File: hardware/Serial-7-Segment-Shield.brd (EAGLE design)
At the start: 59.7 x 53.3 mm, 32 parts, among them J1 AVR_SPI_PRG_6PTH, U1 ARDUINO_SHIELDLABEL

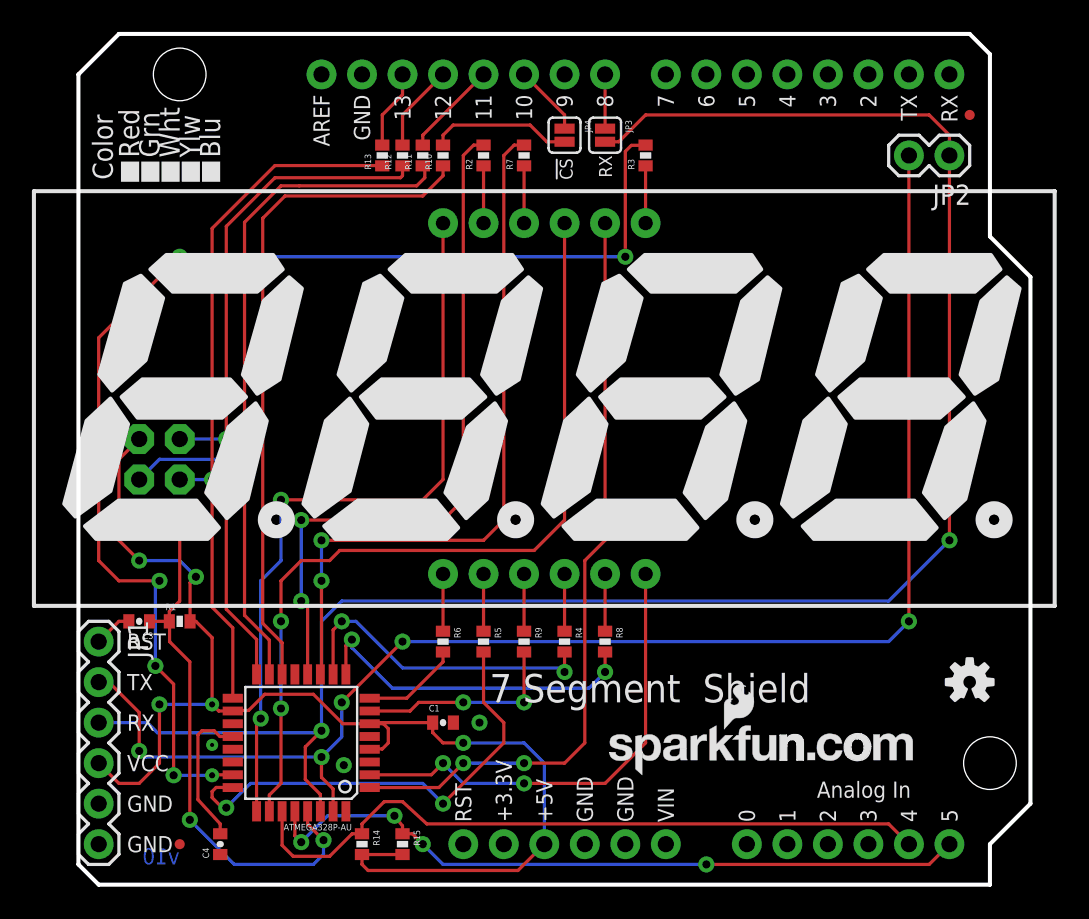
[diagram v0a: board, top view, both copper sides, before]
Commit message: 0603 Cap/Res Change
Changed all caps and res to 0603, minor trace re-routing
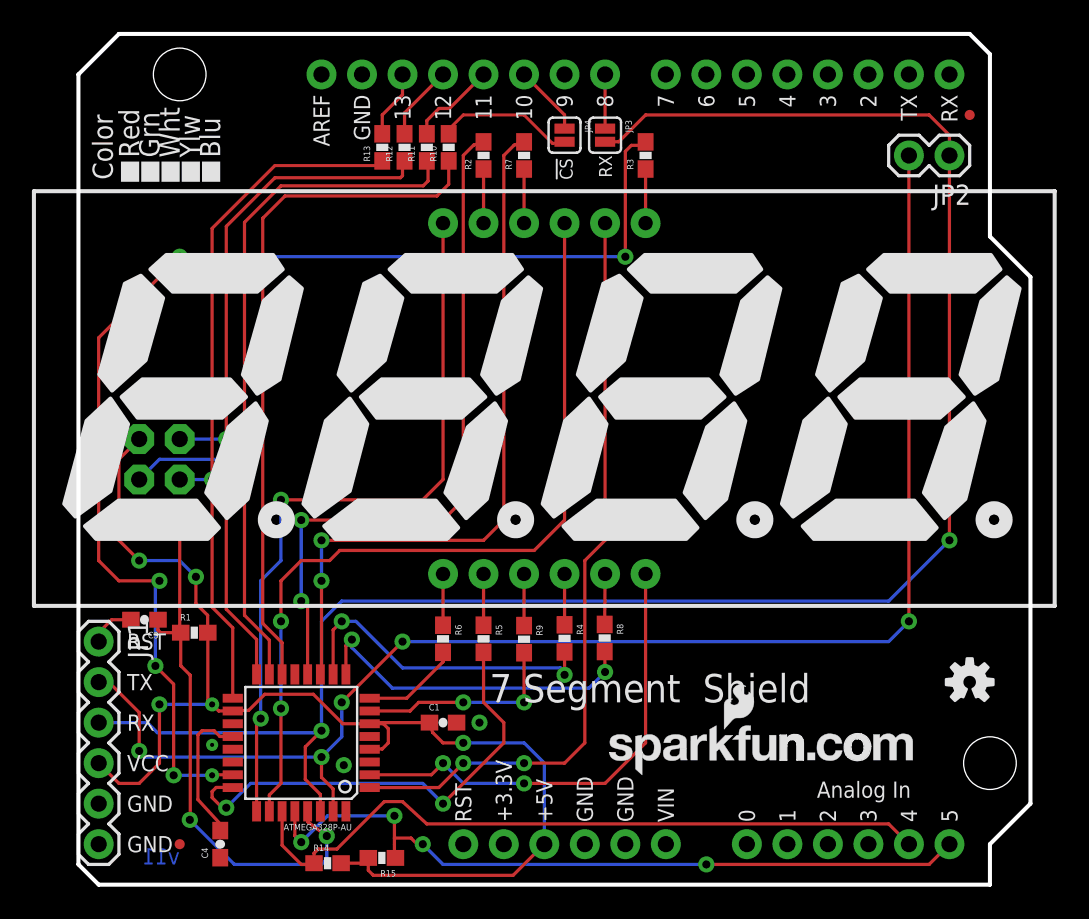
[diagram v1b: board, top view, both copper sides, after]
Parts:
- C1: device SparkFun:0402-CAP -> SparkFun:0603-CAP
- C3, C4: device SparkFun-Passives:0402-CAP -> SparkFun-Passives:0603-CAP
- R1, R10, R11, R12, R13, R14, R15, R2, R3, R4, R5, R6, R7, R8, R9: device SparkFun:0402-RES -> SparkFun:0603-RES
- moved R14 2.47 mm to (15.6, 1.35), turned to 0 degrees
- moved R15 1.56 mm to (19.0, 1.68), turned to 180 degrees
- moved R1 1.16 mm to (7.26, 15.8)
- moved R10 0.62 mm to (23.2, 46.2)
- moved R11 0.57 mm to (21.8, 46.2)
- moved R12 0.52 mm to (20.4, 46.2)
- moved R13 0.51 mm to (19.1, 46.2)
- moved C3 0.35 mm to (4.14, 16.6)
- moved R8 0.23 mm to (33.0, 15.5)
- moved R4 0.20 mm to (30.5, 15.4)
- moved R5 0.18 mm to (25.4, 15.4)
- moved R6 0.18 mm to (22.9, 15.4)
- moved R9 0.15 mm to (27.9, 15.4)
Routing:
- net SCL: track 45.5 -> 47.3 mm
- net VCC: track 81.1 -> 79.6 mm
- net !SS: track 42.1 -> 43.2 mm
- net RESET: track 33.7 -> 34.7 mm
- net N$3: track 5.48 -> 4.72 mm
- net N$2: track 4.96 -> 4.25 mm
- net MOSI: track 49.4 -> 50.0 mm
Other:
- board text added: "v11"
- board text removed: "v10"
